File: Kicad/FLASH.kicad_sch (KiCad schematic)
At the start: 5 parts, among them U10 SST39SF010, U9 29F160

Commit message: PCB: Keep on routing...
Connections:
- net FLASH_A18 renamed A19
- net ~{FLASH_BSY}: no longer names the net of R11.1, U9.15 (~{BSY})
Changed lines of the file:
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@@
 (kicad_sch (version 20211123) (generator eeschema)
   (paper "A4")
-  (junction (at 147.32 109.22) (diameter 0) (color 0 0 0 0)
-  )
   (junction (at 85.725 121.92) (diameter 0) (color 0 0 0 0)
   )
@@
     (stroke (width 0) (type default) (color 0 0 0 0))
   )
+  (bus_entry (at 90.17 110.49) (size 2.54 2.54)
+    (stroke (width 0) (type default) (color 0 0 0 0))
+  )
   (bus_entry (at 181.61 79.375) (size 2.54 2.54)
     (stroke (width 0) (type default) (color 0 0 0 0))
@@
     (stroke (width 0) (type default) (color 0 0 0 0))
   )
+  (wire (pts (xy 92.71 113.03) (xy 99.06 113.03))
+    (stroke (width 0) (type default) (color 0 0 0 0))
+  )
   (wire (pts (xy 184.15 79.375) (xy 187.96 79.375))
     (stroke (width 0) (type default) (color 0 0 0 0))
@@
     (stroke (width 0) (type default) (color 0 0 0 0))
   )
-  (wire (pts (xy 147.32 109.22) (xy 153.67 109.22))
-    (stroke (width 0) (type default) (color 0 0 0 0))
-  )
   (bus (pts (xy 224.79 76.835) (xy 224.79 79.375))
     (stroke (width 0) (type default) (color 0 0 0 0))
@@
     (stroke (width 0) (type default) (color 0 0 0 0))
   )
-  (wire (pts (xy 67.31 113.03) (xy 99.06 113.03))
-    (stroke (width 0) (type default) (color 0 0 0 0))
-  )
   (bus (pts (xy 67.31 52.07) (xy 90.17 52.07))
     (stroke (width 0) (type default) (color 0 0 0 0))
@@
     (stroke (width 0) (type default) (color 0 0 0 0))
   )
+  (bus (pts (xy 90.17 107.95) (xy 90.17 110.49))
+    (stroke (width 0) (type default) (color 0 0 0 0))
+  )
   (wire (pts (xy 111.76 135.89) (xy 113.03 135.89))
     (stroke (width 0) (type default) (color 0 0 0 0))
@@
   (label "D11" (at 218.44 74.295 0)
     (effects (font (size 1.27 1.27)) (justify left bottom))
+  )
+  (label "A19" (at 99.06 113.03 180)
+    (effects (font (size 1.27 1.27)) (justify right bottom))
   )
   (label "D9" (at 218.44 69.215 0)
@@
     (effects (font (size 1.27 1.27)) (justify right))
   )
-  (hierarchical_label "~{FLASH_BSY}" (shape output) (at 153.67 109.22 0)
-    (effects (font (size 1.27 1.27)) (justify left))
-  )
   (hierarchical_label "~{RST}" (shape input) (at 67.31 128.27 180)
     (effects (font (size 1.27 1.27)) (justify right))
@@
     (effects (font (size 1.27 1.27)) (justify right))
   )
-  (hierarchical_label "FLASH_A18" (shape input) (at 67.31 113.03 180)
-    (effects (font (size 1.27 1.27)) (justify right))
-  )

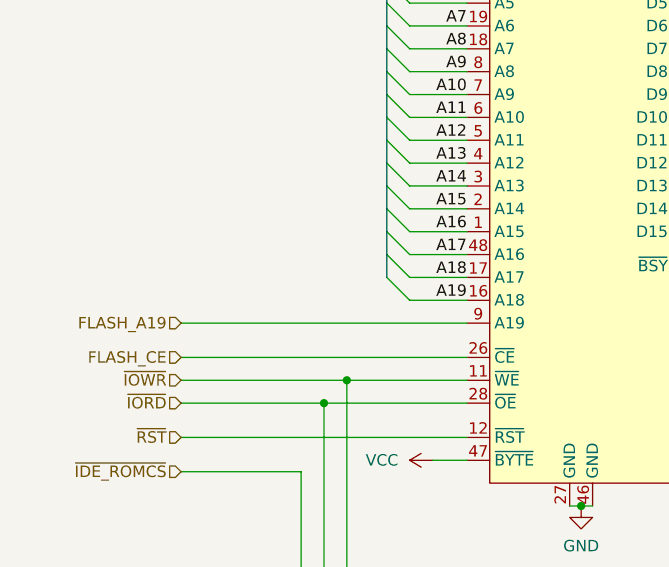
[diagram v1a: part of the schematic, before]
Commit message: PCB: Connect Flash A18 to CPLD
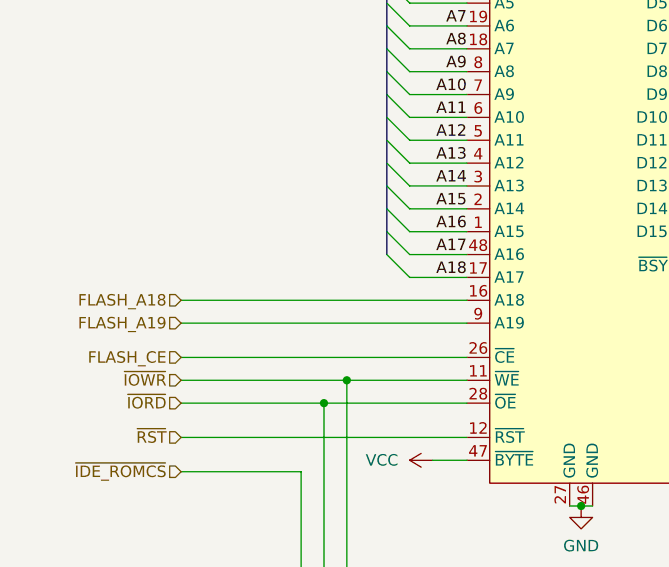
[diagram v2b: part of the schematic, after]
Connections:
- net A19 renamed FLASH_A18
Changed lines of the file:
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@@
-    (stroke (width 0) (type default) (color 0 0 0 0))
-  )
-  (bus_entry (at 90.17 110.49) (size 2.54 2.54)
     (stroke (width 0) (type default) (color 0 0 0 0))
   )
@@
     (stroke (width 0) (type default) (color 0 0 0 0))
   )
+  (wire (pts (xy 67.31 113.03) (xy 99.06 113.03))
+    (stroke (width 0) (type default) (color 0 0 0 0))
+  )
   (bus (pts (xy 133.35 95.25) (xy 133.35 97.79))
     (stroke (width 0) (type default) (color 0 0 0 0))
@@
     (stroke (width 0) (type default) (color 0 0 0 0))
   )
-  (wire (pts (xy 92.71 113.03) (xy 99.06 113.03))
-    (stroke (width 0) (type default) (color 0 0 0 0))
-  )
   (wire (pts (xy 184.15 79.375) (xy 187.96 79.375))
     (stroke (width 0) (type default) (color 0 0 0 0))
@@
     (stroke (width 0) (type default) (color 0 0 0 0))
   )
-  (bus (pts (xy 90.17 107.95) (xy 90.17 110.49))
-    (stroke (width 0) (type default) (color 0 0 0 0))
-  )
   (wire (pts (xy 111.76 135.89) (xy 113.03 135.89))
     (stroke (width 0) (type default) (color 0 0 0 0))
@@
   (label "D11" (at 218.44 74.295 0)
     (effects (font (size 1.27 1.27)) (justify left bottom))
-  )
-  (label "A19" (at 99.06 113.03 180)
-    (effects (font (size 1.27 1.27)) (justify right bottom))
   )
   (label "D9" (at 218.44 69.215 0)
@@
   )
   (hierarchical_label "~{IDE_ROMCS}" (shape input) (at 67.31 132.08 180)
+    (effects (font (size 1.27 1.27)) (justify right))
+  )
+  (hierarchical_label "FLASH_A18" (shape input) (at 67.31 113.03 180)
     (effects (font (size 1.27 1.27)) (justify right))
   )
@@
       (effects (font (size 1.27 1.27)) hide)
     )
-    (property "Datasheet" "http://ww1.microchip.com/downloads/en/DeviceDoc/25022B.pdf" (id 3) (at 203.2 89.535 0)
-      (effects (font (size 1.27 1.27)) hide)
-    )
+    (property "Datasheet" "https://ww1.microchip.com/downloads/aemDocuments/documents/OTH/ProductDocuments/DataSheets/20005022C.pdf" (id 3) (at 203.2 89.535 0)
+      (effects (font (size 1.27 1.27)) hide)
+    )

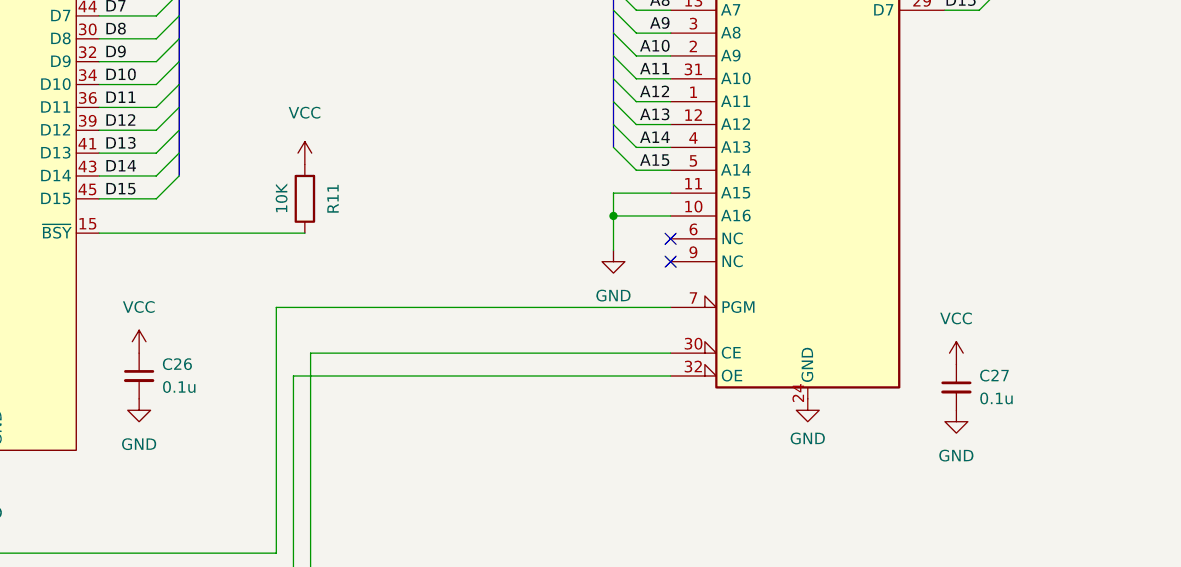
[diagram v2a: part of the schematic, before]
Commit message: PCB: Remove useless cfgin connection
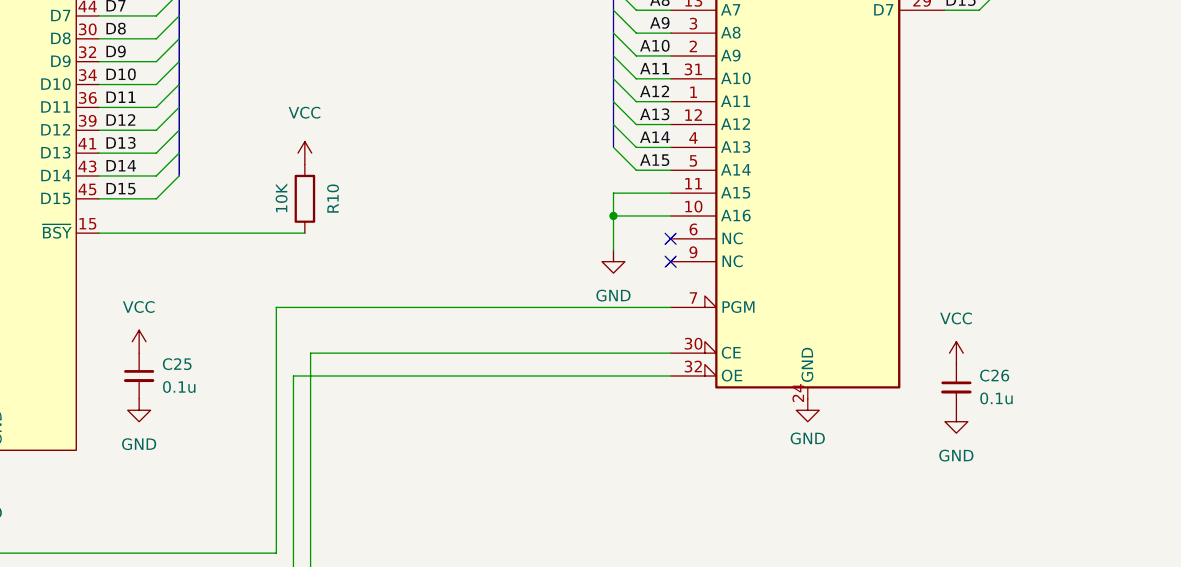
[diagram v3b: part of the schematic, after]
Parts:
- renumbered C26 to C25, C27 to C26, R11 to R10
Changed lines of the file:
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@@
   (symbol (lib_id "power:VCC") (at 219.71 123.825 0) (unit 1)
     (in_bom yes) (on_board yes) (fields_autoplaced)
-    (property "Reference" "#PWR059" (id 0) (at 219.71 127.635 0)
+    (property "Reference" "#PWR058" (id 0) (at 219.71 127.635 0)
       (effects (font (size 1.27 1.27)) hide)
     )
@@
   (symbol (lib_id "Device:R") (at 147.32 105.41 180) (unit 1)
     (in_bom yes) (on_board yes)
-    (property "Reference" "R11" (id 0) (at 150.495 105.41 90))
+    (property "Reference" "R10" (id 0) (at 150.495 105.41 90))
     (property "Value" "10K" (id 1) (at 144.78 105.41 90))
     (property "Footprint" "Resistor_SMD:R_0603_1608Metric" (id 2) (at 149.098 105.41 90)
@@
   (symbol (lib_id "power:GND") (at 219.71 128.905 0) (unit 1)
     (in_bom yes) (on_board yes) (fields_autoplaced)
-    (property "Reference" "#PWR060" (id 0) (at 219.71 135.255 0)
+    (property "Reference" "#PWR059" (id 0) (at 219.71 135.255 0)
       (effects (font (size 1.27 1.27)) hide)
     )
@@
   (symbol (lib_id "power:GND") (at 128.905 127.635 0) (unit 1)
     (in_bom yes) (on_board yes) (fields_autoplaced)
-    (property "Reference" "#PWR055" (id 0) (at 128.905 133.985 0)
+    (property "Reference" "#PWR053" (id 0) (at 128.905 133.985 0)
       (effects (font (size 1.27 1.27)) hide)
     )
@@
   (symbol (lib_id "power:VCC") (at 147.32 101.6 0) (unit 1)
     (in_bom yes) (on_board yes) (fields_autoplaced)
-    (property "Reference" "#PWR053" (id 0) (at 147.32 105.41 0)
+    (property "Reference" "#PWR054" (id 0) (at 147.32 105.41 0)
       (effects (font (size 1.27 1.27)) hide)
     )
@@
   (symbol (lib_id "Device:C_Small") (at 219.71 126.365 0) (unit 1)
     (in_bom yes) (on_board yes) (fields_autoplaced)
-    (property "Reference" "C27" (id 0) (at 222.25 125.0949 0)
+    (property "Reference" "C26" (id 0) (at 222.25 125.0949 0)
       (effects (font (size 1.27 1.27)) (justify left))
     )
@@
   (symbol (lib_id "power:VCC") (at 111.76 62.23 0) (unit 1)
     (in_bom yes) (on_board yes) (fields_autoplaced)
-    (property "Reference" "#PWR051" (id 0) (at 111.76 66.04 0)
+    (property "Reference" "#PWR050" (id 0) (at 111.76 66.04 0)
       (effects (font (size 1.27 1.27)) hide)
     )
@@
   (symbol (lib_id "power:VCC") (at 95.25 130.81 90) (mirror x) (unit 1)
     (in_bom yes) (on_board yes) (fields_autoplaced)
-    (property "Reference" "#PWR050" (id 0) (at 99.06 130.81 0)
+    (property "Reference" "#PWR049" (id 0) (at 99.06 130.81 0)
       (effects (font (size 1.27 1.27)) hide)
     )
@@
   (symbol (lib_id "power:GND") (at 181.61 111.125 0) (unit 1)
     (in_bom yes) (on_board yes) (fields_autoplaced)
-    (property "Reference" "#PWR056" (id 0) (at 181.61 117.475 0)
+    (property "Reference" "#PWR055" (id 0) (at 181.61 117.475 0)
       (effects (font (size 1.27 1.27)) hide)
     )
@@
   (symbol (lib_id "power:GND") (at 111.76 135.89 0) (unit 1)
     (in_bom yes) (on_board yes) (fields_autoplaced)
-    (property "Reference" "#PWR052" (id 0) (at 111.76 142.24 0)
+    (property "Reference" "#PWR051" (id 0) (at 111.76 142.24 0)
       (effects (font (size 1.27 1.27)) hide)
     )
@@
   (symbol (lib_id "Device:C_Small") (at 128.905 125.095 0) (unit 1)
     (in_bom yes) (on_board yes) (fields_autoplaced)
-    (property "Reference" "C26" (id 0) (at 131.445 123.8249 0)
+    (property "Reference" "C25" (id 0) (at 131.445 123.8249 0)
       (effects (font (size 1.27 1.27)) (justify left))
     )
@@
   (symbol (lib_id "power:VCC") (at 128.905 122.555 0) (unit 1)
     (in_bom yes) (on_board yes) (fields_autoplaced)
-    (property "Reference" "#PWR054" (id 0) (at 128.905 126.365 0)
+    (property "Reference" "#PWR052" (id 0) (at 128.905 126.365 0)
       (effects (font (size 1.27 1.27)) hide)
     )
@@
   (symbol (lib_id "power:GND") (at 203.2 127.635 0) (unit 1)
     (in_bom yes) (on_board yes) (fields_autoplaced)
-    (property "Reference" "#PWR058" (id 0) (at 203.2 133.985 0)
+    (property "Reference" "#PWR057" (id 0) (at 203.2 133.985 0)
       (effects (font (size 1.27 1.27)) hide)
     )
@@
   (symbol (lib_id "power:VCC") (at 203.2 64.135 0) (unit 1)
     (in_bom yes) (on_board yes) (fields_autoplaced)
-    (property "Reference" "#PWR057" (id 0) (at 203.2 67.945 0)
-      (effects (font (size 1.27 1.27)) hide)
-    )
+    (property "Reference" "#PWR056" (id 0) (at 203.2 67.945 0)
+      (effects (font (size 1.27 1.27)) hide)
+    )

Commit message: PCB: Fixups
* Tweak KEL connector hole sizes
* Fixup MT48LC8M16A2P - Had copied this from the 16M16 part and forgot to make A12 an NC
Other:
- company: (none) -> Matt Harlum
- title: (none) -> CIDER
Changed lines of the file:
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@@
 (kicad_sch (version 20211123) (generator eeschema)
   (paper "A4")
+  (title_block
+    (title "CIDER")
+    (company "Matt Harlum")
+  )
   (junction (at 85.725 121.92) (diameter 0) (color 0 0 0 0)
   )

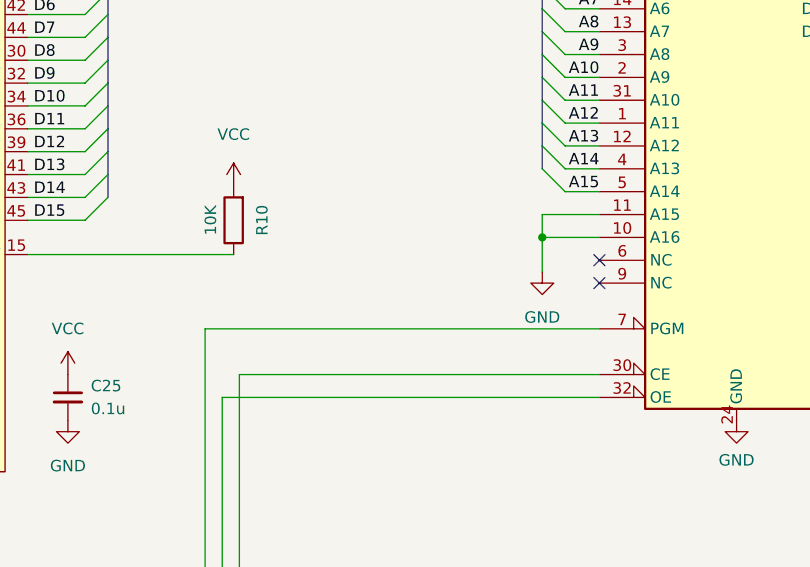
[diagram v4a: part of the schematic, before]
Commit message: PCB: Connect NC's of 39SF010 to GND
This will allow people to substitute 39SF020/040 if the 010 ever becomes unobtanium
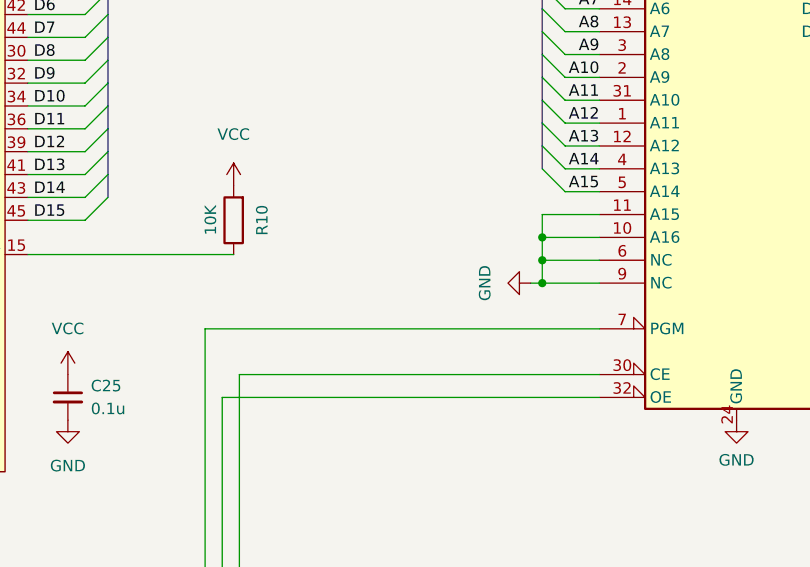
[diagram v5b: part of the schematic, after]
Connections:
- net GND: now also U10.6 (NC), U10.9 (NC)
- no-connect marks 2 -> 0
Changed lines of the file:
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@@
   (junction (at 85.725 121.92) (diameter 0) (color 0 0 0 0)
   )
+  (junction (at 181.61 109.855) (diameter 0) (color 0 0 0 0)
+  )
   (junction (at 224.79 50.165) (diameter 0) (color 0 0 0 0)
   )
@@
   (junction (at 181.61 107.315) (diameter 0) (color 0 0 0 0)
   )
-  (no_connect (at 187.96 112.395))
-  (no_connect (at 187.96 109.855))
+  (junction (at 181.61 112.395) (diameter 0) (color 0 0 0 0)
+  )
   (bus_entry (at 90.17 72.39) (size 2.54 2.54)
     (stroke (width 0) (type default) (color 0 0 0 0))
@@
     (stroke (width 0) (type default) (color 0 0 0 0))
   )
+  (wire (pts (xy 181.61 109.855) (xy 181.61 112.395))
+    (stroke (width 0) (type default) (color 0 0 0 0))
+  )
   (wire (pts (xy 184.15 79.375) (xy 187.96 79.375))
     (stroke (width 0) (type default) (color 0 0 0 0))
@@
     (stroke (width 0) (type default) (color 0 0 0 0))
   )
+  (wire (pts (xy 144.145 117.475) (xy 187.96 117.475))
+    (stroke (width 0) (type default) (color 0 0 0 0))
+  )
   (wire (pts (xy 184.15 97.155) (xy 187.96 97.155))
     (stroke (width 0) (type default) (color 0 0 0 0))
   )
+  (wire (pts (xy 181.61 109.855) (xy 187.96 109.855))
+    (stroke (width 0) (type default) (color 0 0 0 0))
+  )
   (wire (pts (xy 147.955 122.555) (xy 147.955 148.59))
     (stroke (width 0) (type default) (color 0 0 0 0))
@@
     (stroke (width 0) (type default) (color 0 0 0 0))
   )
-  (wire (pts (xy 187.96 117.475) (xy 144.145 117.475))
-    (stroke (width 0) (type default) (color 0 0 0 0))
-  )
   (wire (pts (xy 146.05 125.095) (xy 146.05 146.685))
     (stroke (width 0) (type default) (color 0 0 0 0))
@@
     (stroke (width 0) (type default) (color 0 0 0 0))
   )
+  (wire (pts (xy 180.34 112.395) (xy 181.61 112.395))
+    (stroke (width 0) (type default) (color 0 0 0 0))
+  )
+  (wire (pts (xy 181.61 112.395) (xy 187.96 112.395))
+    (stroke (width 0) (type default) (color 0 0 0 0))
+  )
   (bus (pts (xy 133.35 92.71) (xy 133.35 95.25))
     (stroke (width 0) (type default) (color 0 0 0 0))
@@
     (stroke (width 0) (type default) (color 0 0 0 0))
   )
-  (wire (pts (xy 181.61 107.315) (xy 181.61 111.125))
+  (wire (pts (xy 181.61 107.315) (xy 181.61 109.855))
     (stroke (width 0) (type default) (color 0 0 0 0))
   )
@@
     (pin "1")
   )
-  (symbol (lib_id "power:GND") (at 181.61 111.125 0) (unit 1)
+  (symbol (lib_id "power:GND") (at 180.34 112.395 270) (unit 1)
     (in_bom yes) (on_board yes) (fields_autoplaced)
-    (property "Reference" "#PWR055" (id 0) (at 181.61 117.475 0)
-      (effects (font (size 1.27 1.27)) hide)
-    )
-    (property "Value" "GND" (id 1) (at 181.61 116.205 0))
-    (property "Footprint" "" (id 2) (at 181.61 111.125 0)
-      (effects (font (size 1.27 1.27)) hide)
-    )
-    (property "Datasheet" "" (id 3) (at 181.61 111.125 0)
-      (effects (font (size 1.27 1.27)) hide)
-    )
+    (property "Reference" "#PWR055" (id 0) (at 173.99 112.395 0)
+      (effects (font (size 1.27 1.27)) hide)
+    )
+    (property "Value" "GND" (id 1) (at 175.26 112.395 0))
+    (property "Footprint" "" (id 2) (at 180.34 112.395 0)
+      (effects (font (size 1.27 1.27)) hide)
+    )
+    (property "Datasheet" "" (id 3) (at 180.34 112.395 0)
+      (effects (font (size 1.27 1.27)) hide)
+    )
